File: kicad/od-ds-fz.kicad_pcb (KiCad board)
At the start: 2 copper layers, 42 parts, among them J1 AudioJack2, J2 AudioJack2, U1 TLC274

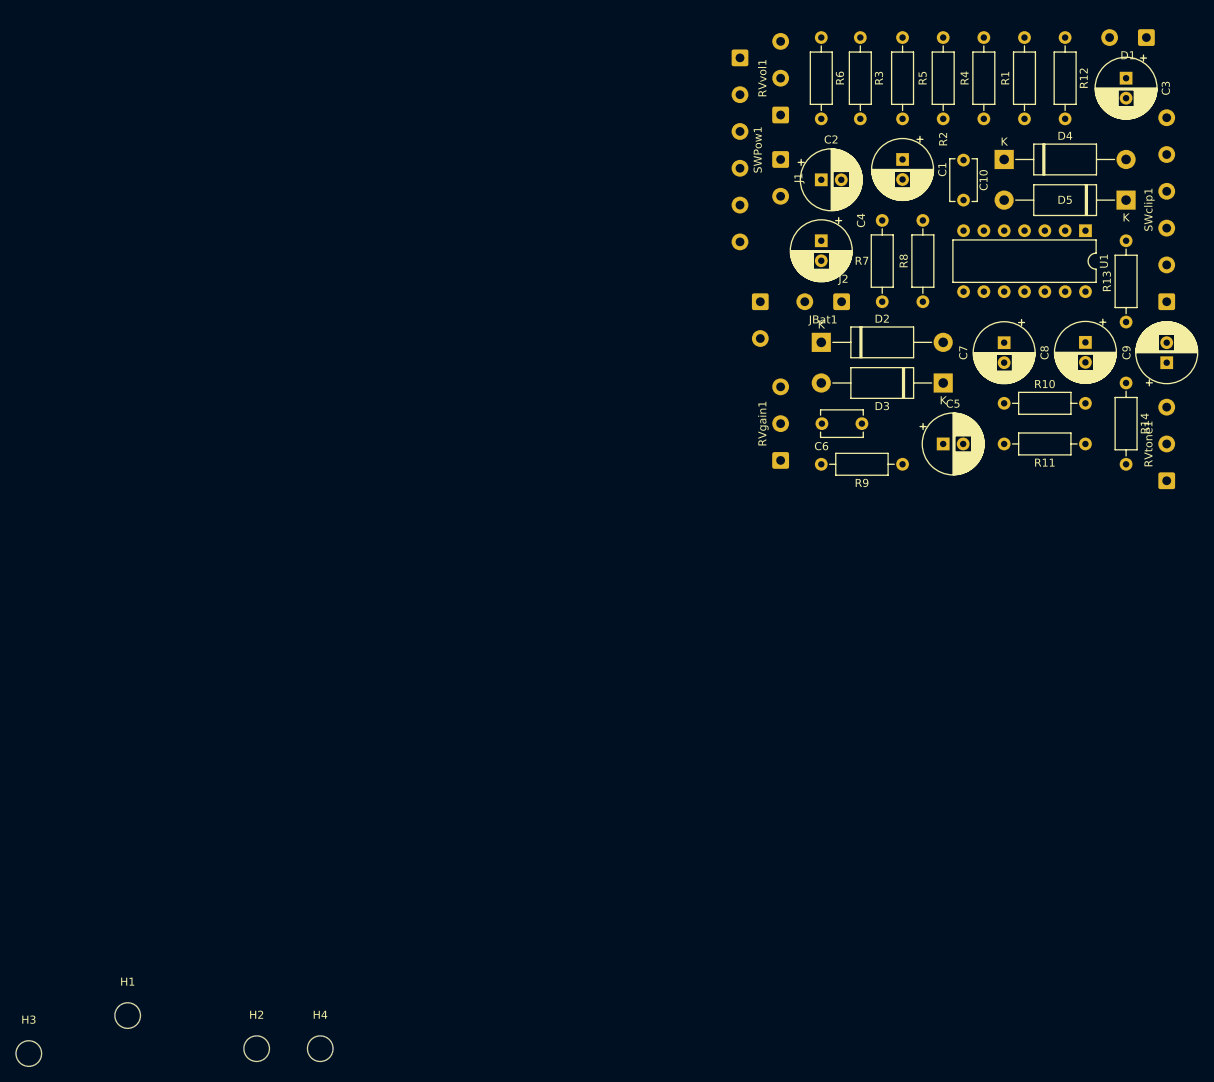
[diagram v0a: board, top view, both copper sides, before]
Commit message: Placed mounting holes
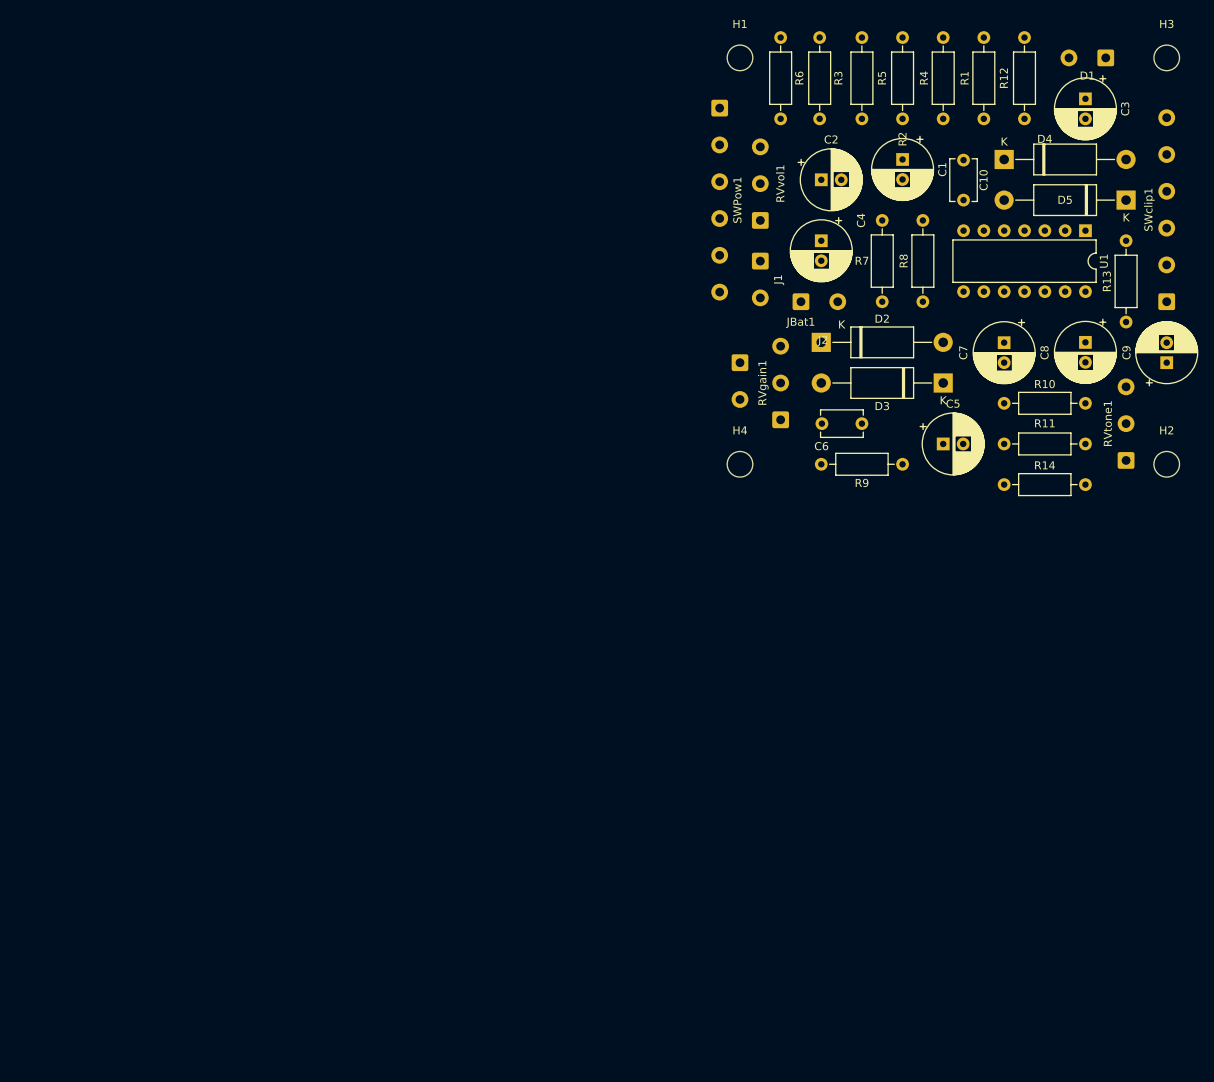
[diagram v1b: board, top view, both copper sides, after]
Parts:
- moved H3 189.0 mm to (175.3, 61.0)
- moved H1 142.1 mm to (121.9, 61.0)
- moved H2 135.2 mm to (175.3, 111.8)
- moved H4 89.9 mm to (121.9, 111.8)
- moved R14 19.8 mm to (154.9, 114.3), turned to 0 degrees
- moved RVvol1 13.4 mm to (124.5, 81.3)
- moved J1 13.0 mm to (124.5, 86.4)
- moved J2 8.03 mm to (121.9, 99.1)
- moved SWPow1 6.77 mm to (119.4, 67.2)
- moved C3 5.70 mm to (165.1, 66.1)
- moved D1 5.68 mm to (167.6, 61.0)
- moved RVtone1 5.68 mm to (170.2, 111.3)
- moved JBat1 5.08 mm to (129.5, 91.4), turned to 0 degrees
- moved R12 5.08 mm to (157.5, 58.4)
- moved R2 5.08 mm to (137.2, 58.4)
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
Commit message: Precise placement
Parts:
- moved J2 31.9 mm to (127.0, 67.5)
- moved RVvol1 14.6 mm to (130.8, 68.1)
- moved J1 9.02 mm to (127.0, 77.7)
- moved RVgain1 8.89 mm to (127.0, 97.3)
- moved R6 7.52 mm to (134.5, 58.4)
- moved R3 6.45 mm to (138.3, 58.4)
- moved R14 5.68 mm to (152.4, 109.2)
- moved SWPow1 5.44 mm to (123.2, 71.1)
- moved R2 4.98 mm to (142.1, 58.4)
- moved H2 4.58 mm to (172.7, 108.0)
- moved H4 4.58 mm to (124.5, 108.0)
- moved R11 4.58 mm to (162.6, 105.4)
- moved C9 4.02 mm to (171.4, 97.8)
- moved RVtone1 4.02 mm to (166.4, 110.0)
- moved R5 3.81 mm to (146.1, 58.4)
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
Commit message: routing and output files
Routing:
- net Net-(C6-Pad1): track 0.00 -> 65.3 mm
- net Net-(C6-Pad2): track 0.00 -> 49.0 mm
- net /in: track 0.00 -> 47.4 mm
- net /Vhigh: track 0.00 -> 46.8 mm
- net Net-(R13-Pad2): track 0.00 -> 43.2 mm
- net Net-(C8-Pad2): track 0.00 -> 41.6 mm
- net /opamp4in: track 0.00 -> 38.3 mm
- net Net-(D2-Pad2): track 0.00 -> 35.3 mm
- net /Vmid: track 0.00 -> 34.6 mm
- net Net-(C2-Pad1): track 0.00 -> 30.3 mm
- net Net-(C8-Pad1): track 0.00 -> 28.5 mm
- net Net-(SWPow1-Pad5): track 0.00 -> 26.4 mm
- net Net-(R14-Pad1): track 0.00 -> 26.0 mm
- net Net-(RVvol1-Pad2): track 0.00 -> 24.8 mm
- net Net-(C9-Pad1): track 0.00 -> 22.7 mm
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- added copper zone on B.Cu, net GND
- added copper zone on F.Cu, net GND
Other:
- board outline added: 57.1 x 55.9 mm
- board text added: "OD-DS-FZ v0.0.0"
